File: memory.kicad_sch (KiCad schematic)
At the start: 12 parts, among them U2 SN74LS00DR, U3 HM530281R, U4 HM530281R, U5 HM530281R, U6 HM530281R

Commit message: initial work on layout
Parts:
- added C61: 100n, tbc:C0603, symbol tbc:GCJ188R71H104KA12D
- U2: value SN74LS00DR -> SN74HC00DR; footprint (none) -> tbc:SOIC-14; symbol tbc:SN74LS00DR -> tbc:SN74HC00DR; Mouser 595-SN74LS00DR -> 595-SN74HC00DR
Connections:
- net +5V: now also C61.2
- net GND: now also C61.1
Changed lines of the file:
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@@
   (junction (at 146.05 127) (diameter 0) (color 0 0 0 0)
+  )
+  (junction (at 46.99 97.79) (diameter 0) (color 0 0 0 0)
   )
   (junction (at 133.35 184.15) (diameter 0) (color 0 0 0 0)
@@
     (stroke (width 0) (type default))
   )
+  (wire (pts (xy 31.75 97.79) (xy 35.56 97.79))
+    (stroke (width 0) (type default))
+  )
   (bus (pts (xy 176.53 29.21) (xy 176.53 31.75))
     (stroke (width 0) (type default))
@@
     (stroke (width 0) (type default))
   )
-  (wire (pts (xy 58.42 111.76) (xy 58.42 93.98))
+  (wire (pts (xy 58.42 111.76) (xy 58.42 90.17))
     (stroke (width 0) (type default))
   )
@@
     (stroke (width 0) (type default))
   )
-  (wire (pts (xy 46.99 101.6) (xy 46.99 102.87))
+  (wire (pts (xy 46.99 97.79) (xy 46.99 102.87))
     (stroke (width 0) (type default))
   )
@@
     (stroke (width 0) (type default))
   )
-  (wire (pts (xy 58.42 93.98) (xy 21.59 93.98))
+  (wire (pts (xy 58.42 90.17) (xy 21.59 90.17))
     (stroke (width 0) (type default))
   )
@@
     (stroke (width 0) (type default))
   )
+  (wire (pts (xy 43.18 97.79) (xy 46.99 97.79))
+    (stroke (width 0) (type default))
+  )
   (bus (pts (xy 96.52 36.83) (xy 96.52 39.37))
     (stroke (width 0) (type default))
@@
     (stroke (width 0) (type default))
   )
+  (wire (pts (xy 46.99 96.52) (xy 46.99 97.79))
+    (stroke (width 0) (type default))
+  )
   (wire (pts (xy 165.1 93.98) (xy 171.45 93.98))
     (stroke (width 0) (type default))
@@
     (stroke (width 0) (type default))
   )
-  (wire (pts (xy 21.59 93.98) (xy 21.59 120.65))
+  (wire (pts (xy 21.59 90.17) (xy 21.59 120.65))
     (stroke (width 0) (type default))
   )
@@
   )
   (wire (pts (xy 101.6 215.9) (xy 107.95 215.9))
+    (stroke (width 0) (type default))
+  )
+  (wire (pts (xy 31.75 97.79) (xy 31.75 99.06))
     (stroke (width 0) (type default))
   )
@@
     )
   )
-  (symbol (lib_id "tbc:SN74LS00DR") (at 46.99 121.92 0) (unit 1)
-    (in_bom yes) (on_board yes) (dnp no)
-    (property "Reference" "U2" (at 40.005 103.505 0)
+  (symbol (lib_id "tbc:SN74HC00DR") (at 46.99 121.92 0) (unit 1)
+    (in_bom yes) (on_board yes) (dnp no)
+    (property "Reference" "U2" (at 39.37 104.14 0)
       (effects (font (size 1.27 1.27)) (justify left))
     )
-    (property "Value" "SN74LS00DR" (at 49.53 142.24 0)
+    (property "Value" "SN74HC00DR" (at 49.53 142.24 0)
       (effects (font (size 1.27 1.27)) (justify left))
     )
-    (property "Footprint" "" (at 38.1 109.22 0)
-      (effects (font (size 1.27 1.27)) hide)
-    )
-    (property "Datasheet" "https://www.ti.com/lit/ds/symlink/sn7400.pdf" (at 46.99 156.21 0) (show_name)
-      (effects (font (size 1.27 1.27)) hide)
-    )
-    (property "Mouser" " 595-SN74LS00DR" (at 46.99 158.75 0) (show_name)
-      (effects (font (size 1.27 1.27)) hide)
-    )
-    (property "Sim.Enable" "0" (at 46.99 121.92 0)
+    (property "Footprint" "tbc:SOIC-14" (at 38.1 109.22 0)
+      (effects (font (size 1.27 1.27)) hide)
+    )
+    (property "Datasheet" "https://www.ti.com/lit/gpn/sn74hc00" (at 46.99 156.21 0) (show_name)
+      (effects (font (size 1.27 1.27)) hide)
+    )
+    (property "Mouser" " 595-SN74HC00DR" (at 46.99 158.75 0) (show_name)
+      (effects (font (size 1.27 1.27)) hide)
+    )
+    (property "Sim.Enable" "0" (at 46.99 121.92 0) (show_name)
       (effects (font (size 1.27 1.27)) hide)
     )
@@
         (path "/9df71e53-7941-4fd3-a17d-93619e4e3e02/9336a744-46c0-44d0-bb63-d5b7d4716bcc"
           (reference "#PWR054") (unit 1)
+        )
+      )
+    )
+  )
+  (symbol (lib_id "tbc:GND") (at 31.75 99.06 0) (unit 1)
+    (in_bom yes) (on_board yes) (dnp no)
+    (property "Reference" "#PWR089" (at 31.75 105.41 0)
+      (effects (font (size 1.27 1.27)) hide)
+    )
+    (property "Value" "GND" (at 31.75 102.87 0)
+      (effects (font (size 1.27 1.27)))
+    )
+    (property "Footprint" "" (at 31.75 99.06 0)
+      (effects (font (size 1.27 1.27)) hide)
+    )
+    (property "Datasheet" "" (at 31.75 99.06 0)
+      (effects (font (size 1.27 1.27)) hide)
+    )
+    (property "Sim.Enable" "0" (at 31.75 99.06 0)
+      (effects (font (size 1.27 1.27)) hide)
+    )
+    (pin "1")
+    (instances
+      (project "tbc"
+        (path "/9df71e53-7941-4fd3-a17d-93619e4e3e02/9336a744-46c0-44d0-bb63-d5b7d4716bcc"
+          (reference "#PWR089") (unit 1)
         )
       )
@@
     )
   )
+  (symbol (lib_id "tbc:GCJ188R71H104KA12D") (at 39.37 97.79 0) (unit 1)
+    (in_bom yes) (on_board yes) (dnp no)
+    (property "Reference" "C61" (at 34.29 96.52 0)
+      (effects (font (size 1.27 1.27)))
+    )
+    (property "Value" "100n" (at 39.37 101.6 0)
+      (effects (font (size 1.27 1.27)))
+    )
+    (property "Footprint" "tbc:C0603" (at 39.37 109.22 0)
+      (effects (font (size 1.27 1.27)) hide)
+    )
+    (property "Datasheet" "https://au.mouser.com/datasheet/2/281/1/GCJ188R71H104KA12_02B-3140350.pdf" (at 25.4 110.49 0) (show_name)
+      (effects (font (size 1.27 1.27)) (justify left) hide)
+    )
+    (property "Mouser" " 81-GCJ188R71H104KA2D" (at 25.4 107.95 0) (show_name)
+      (effects (font (size 1.27 1.27)) (justify left) hide)
+    )
+    (property "Sim.Enable" "0" (at 39.37 97.79 0)
+      (effects (font (size 1.27 1.27)) hide)
+    )
+    (pin "1")
+    (pin "2")
+    (instances
+      (project "tbc"
+        (path "/9df71e53-7941-4fd3-a17d-93619e4e3e02/9336a744-46c0-44d0-bb63-d5b7d4716bcc"
+          (reference "C61") (unit 1)
+        )
+      )
+    )
+  )
   (symbol (lib_id "tbc:RC0603FR-0710KL") (at 40.64 195.58 90) (unit 1)
     (in_bom yes) (on_board yes) (dnp no) (fields_autoplaced)
@@
     )
   )
-  (symbol (lib_id "tbc:+5V") (at 46.99 101.6 0) (unit 1)
-    (in_bom yes) (on_board yes) (dnp no)
-    (property "Reference" "#PWR058" (at 46.99 111.76 0)
-      (effects (font (size 1.27 1.27)) hide)
-    )
-    (property "Value" "+5V" (at 46.99 97.79 0)
-      (effects (font (size 1.27 1.27)))
-    )
-    (property "Footprint" "" (at 46.99 101.6 0)
-      (effects (font (size 1.27 1.27)) hide)
-    )
-    (property "Datasheet" "" (at 46.99 101.6 0)
-      (effects (font (size 1.27 1.27)) hide)
-    )
-    (property "Sim.Enable" "0" (at 46.99 101.6 0)
-      (effects (font (size 1.27 1.27)) hide)
-    )
+  (symbol (lib_id "tbc:+5V") (at 46.99 96.52 0) (unit 1)
+    (in_bom yes) (on_board yes) (dnp no)
+    (property "Reference" "#PWR058" (at 46.99 106.68 0)
+      (effects (font (size 1.27 1.27)) hide)
+    )
+    (property "Value" "+5V" (at 46.99 92.71 0)
+      (effects (font (size 1.27 1.27)))
+    )
+    (property "Footprint" "" (at 46.99 96.52 0)
+      (effects (font (size 1.27 1.27)) hide)
+    )
+    (property "Datasheet" "" (at 46.99 96.52 0)
+      (effects (font (size 1.27 1.27)) hide)
+    )
+    (property "Sim.Enable" "0" (at 46.99 96.52 0)
+      (effects (font (size 1.27 1.27)) hide)
+    )

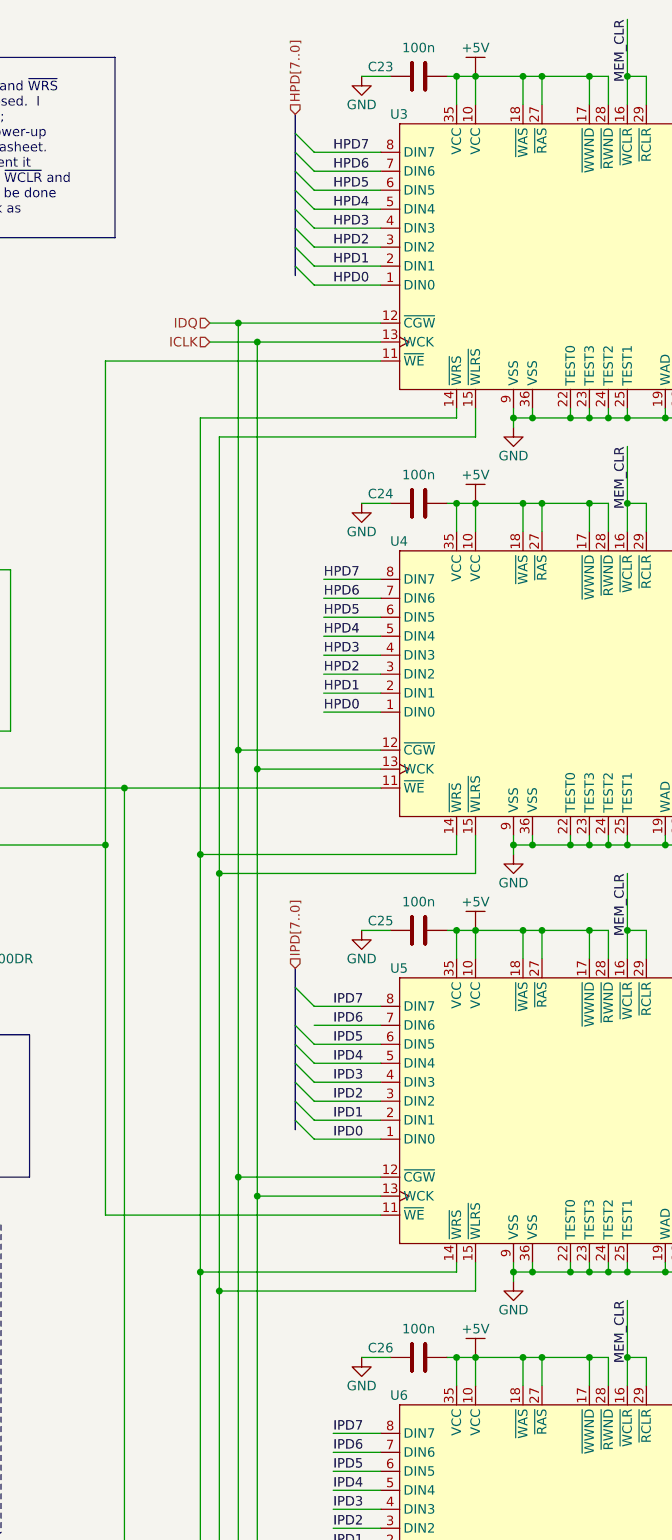
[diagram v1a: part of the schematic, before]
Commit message: extra bypass cap for memories + more layout
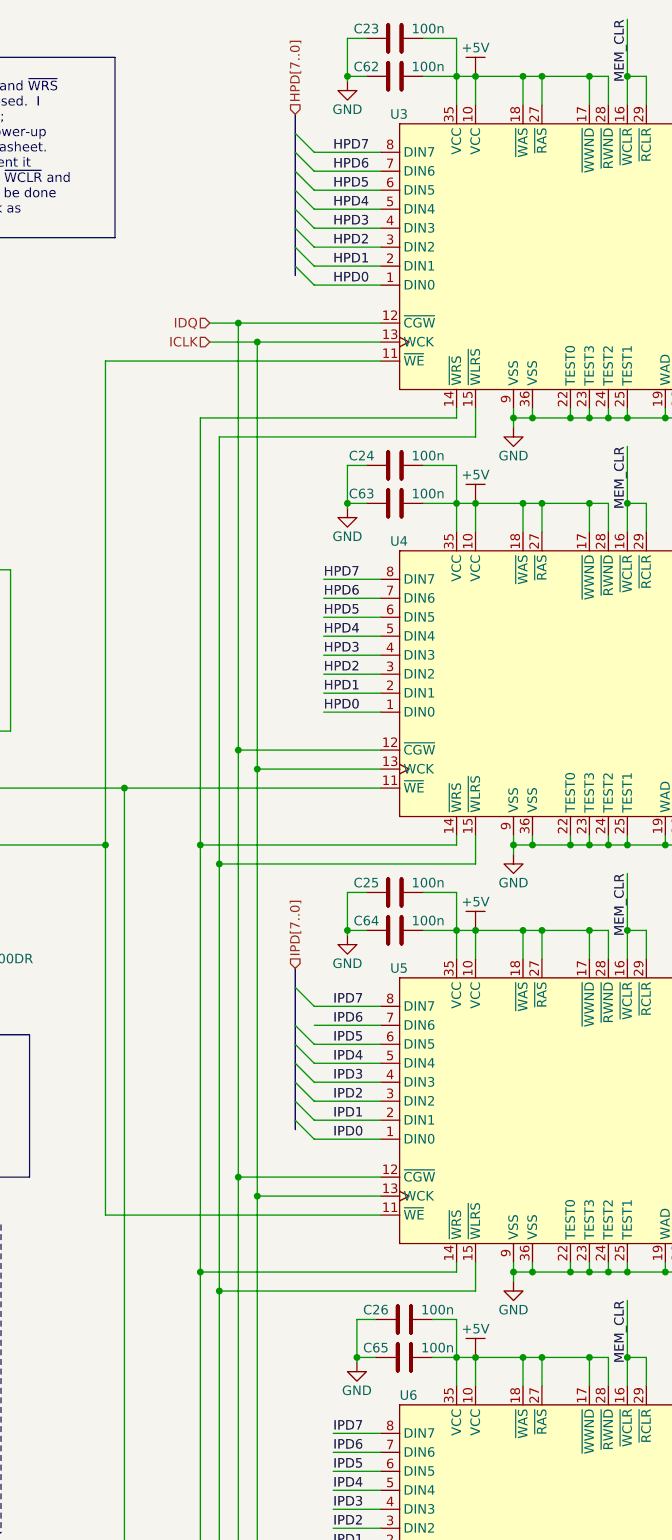
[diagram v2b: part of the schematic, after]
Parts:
- added C62, C63, C64, C65: 100n, tbc:C0603, symbol tbc:GCJ188R71H104KA12D
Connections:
- net +5V: now also C62.2, C63.2, C64.2, C65.2
- net GND: now also C62.1, C63.1, C64.1, C65.1
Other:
- moved on the sheet: C26

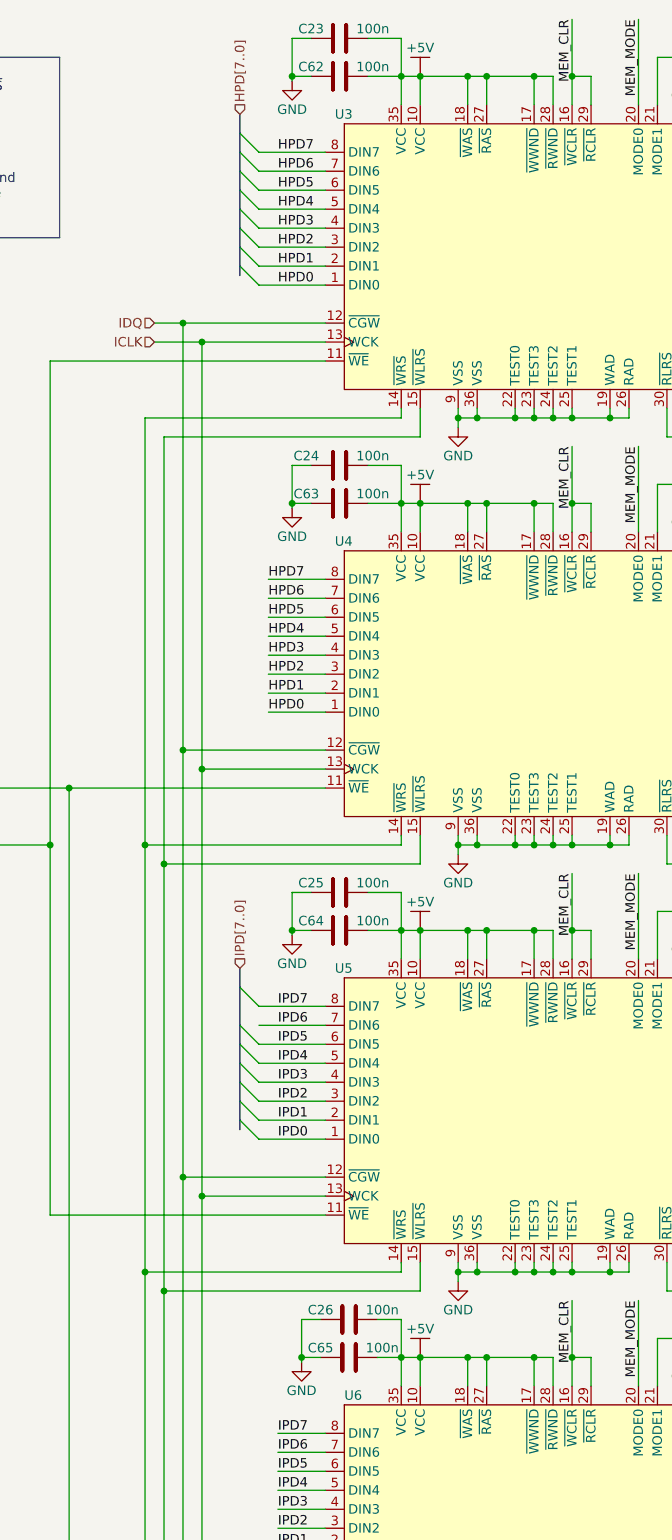
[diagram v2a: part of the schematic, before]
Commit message: update to Kicad 8.0, add gerbers
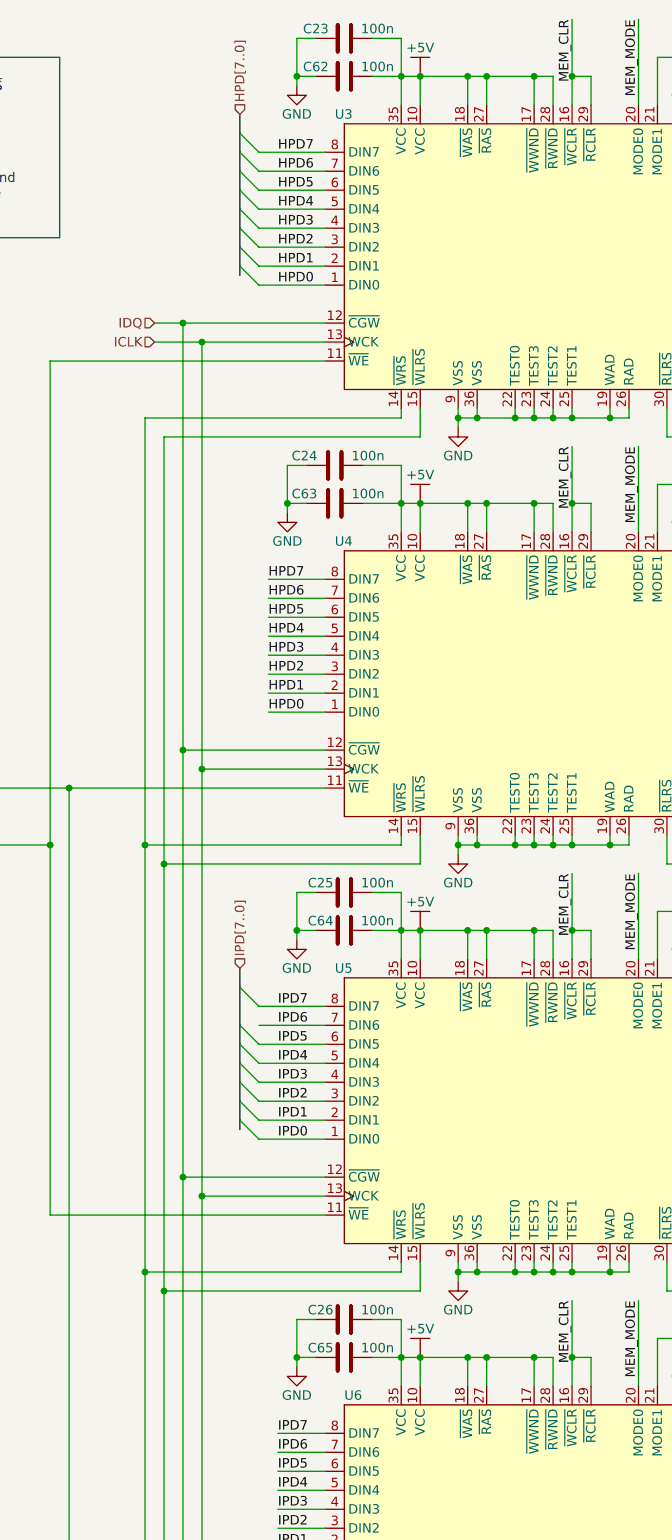
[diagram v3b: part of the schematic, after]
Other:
- moved on the sheet: C23, C24, C25, C26, C62, C63, C64, C65
